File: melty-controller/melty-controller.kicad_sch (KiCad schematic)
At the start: 33 parts, among them J1 Conn_01x02_Male, J2 soicbite, J3 esc_io, Q1 2N7002ET1G, U1 ESP32-PICO-D4, U2 AIC1734-33GUTR, U3 MMA1200KEG, U4 HT7250

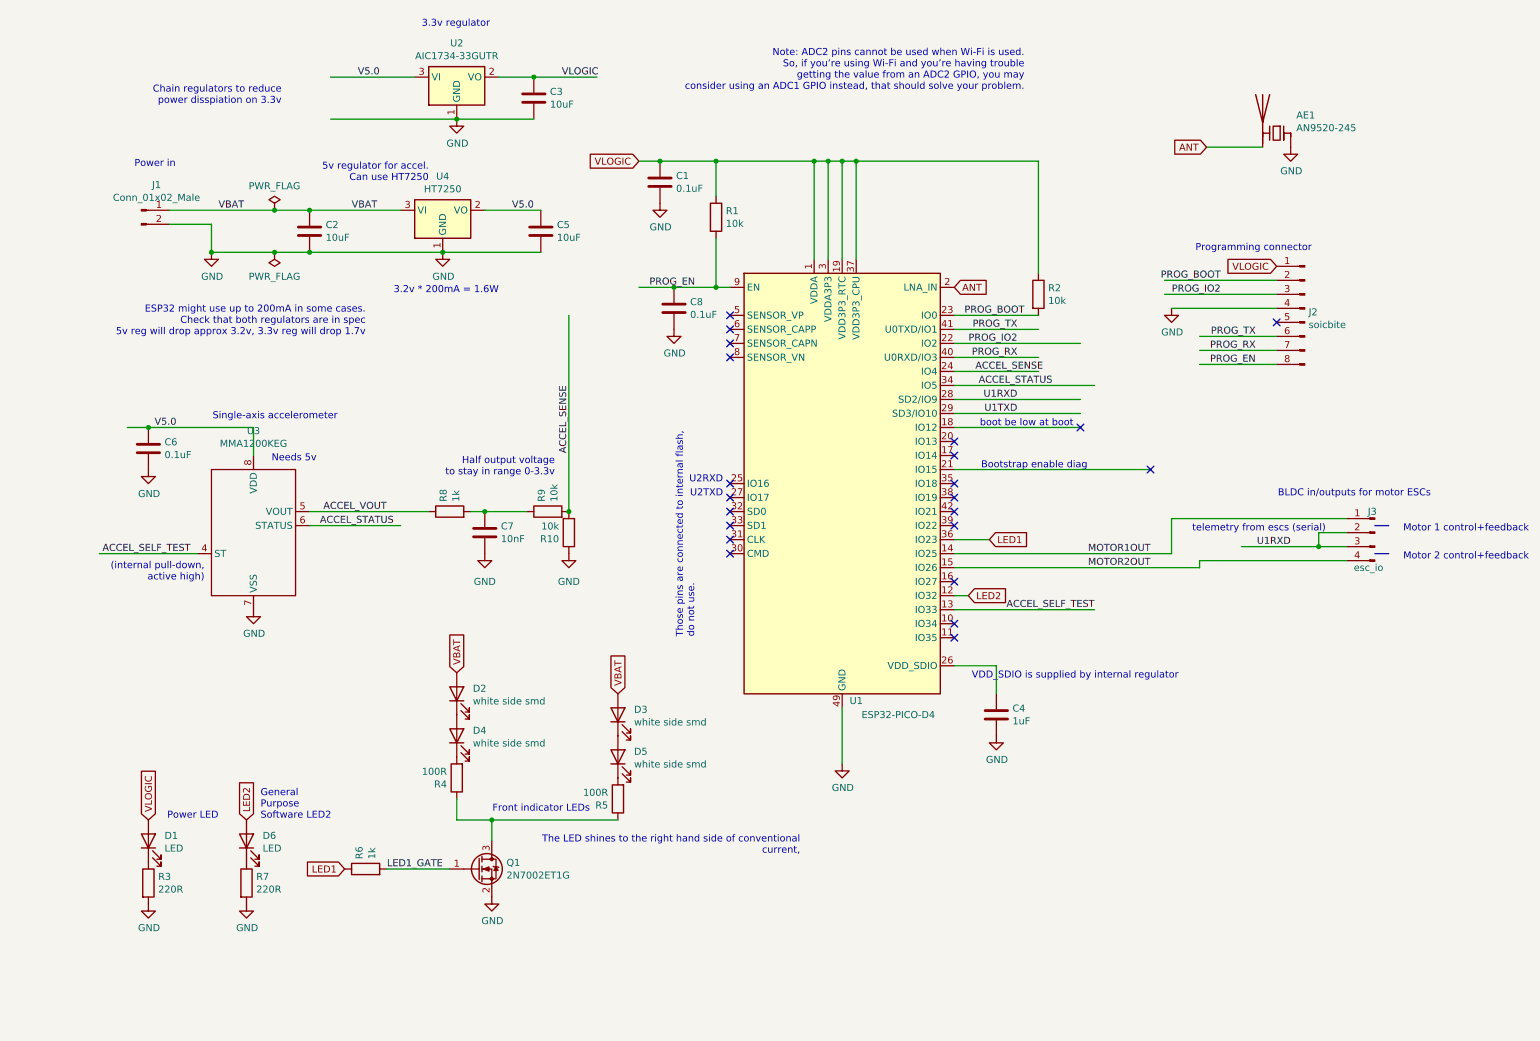
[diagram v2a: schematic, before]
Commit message: clean up net names and stuff
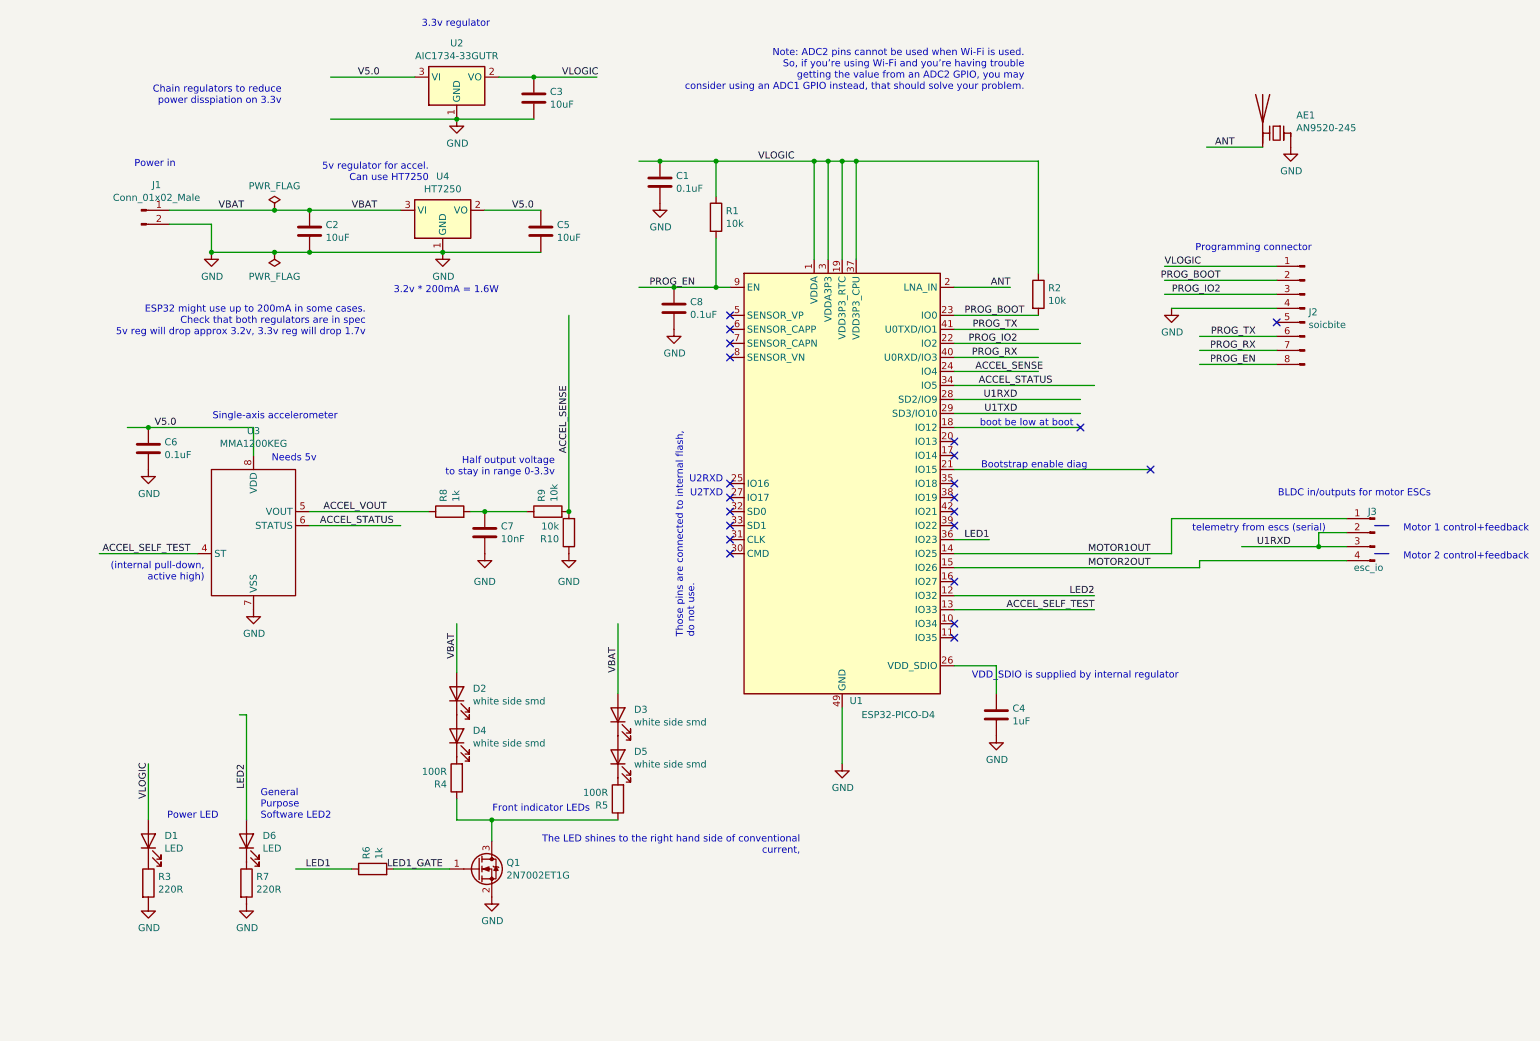
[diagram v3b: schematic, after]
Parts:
- U1: footprint Package_DFN_QFN:QFN-48-1EP_7x7mm_P0.5mm_EP5.3x5.3mm -> melty-controller:esp32-pico-special
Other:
- moved on the sheet: R6
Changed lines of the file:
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@@
   (junction (at 153.67 40.64) (diameter 0) (color 0 0 0 0))
   (junction (at 237.49 110.49) (diameter 0) (color 0 0 0 0))
+  (no_connect (at 130.81 71.12))
+  (no_connect (at 171.45 91.44))
+  (no_connect (at 171.45 116.84))
+  (no_connect (at 229.87 69.85))
+  (no_connect (at 171.45 104.14))
+  (no_connect (at 130.81 73.66))
+  (no_connect (at 171.45 93.98))
+  (no_connect (at 171.45 101.6))
+  (no_connect (at 130.81 106.68))
+  (no_connect (at 171.45 124.46))
+  (no_connect (at 130.81 109.22))
+  (no_connect (at 171.45 127))
+  (no_connect (at 130.81 111.76))
+  (no_connect (at 130.81 68.58))
+  (no_connect (at 130.81 99.06))
+  (no_connect (at 130.81 101.6))
+  (no_connect (at 130.81 104.14))
+  (no_connect (at 171.45 99.06))
+  (no_connect (at 171.45 106.68))
+  (no_connect (at 130.81 76.2))
   (no_connect (at 207.01 96.52))
-  (no_connect (at 130.81 104.14))
-  (no_connect (at 171.45 127))
-  (no_connect (at 171.45 93.98))
-  (no_connect (at 130.81 71.12))
-  (no_connect (at 130.81 106.68))
-  (no_connect (at 130.81 99.06))
-  (no_connect (at 171.45 116.84))
-  (no_connect (at 130.81 111.76))
-  (no_connect (at 130.81 101.6))
-  (no_connect (at 171.45 99.06))
-  (no_connect (at 229.87 69.85))
-  (no_connect (at 171.45 106.68))
-  (no_connect (at 171.45 91.44))
-  (no_connect (at 171.45 101.6))
   (no_connect (at 194.31 88.9))
-  (no_connect (at 130.81 73.66))
-  (no_connect (at 130.81 68.58))
-  (no_connect (at 171.45 104.14))
-  (no_connect (at 130.81 109.22))
-  (no_connect (at 171.45 124.46))
-  (no_connect (at 130.81 76.2))
   (wire (pts (xy 16.51 111.76) (xy 34.29 111.76))
     (stroke (width 0) (type solid) (color 0 0 0 0))
@@
     (stroke (width 0) (type solid) (color 0 0 0 0))
   )
+  (wire (pts (xy 25.4 149.86) (xy 25.4 160.02))
+    (stroke (width 0) (type solid) (color 0 0 0 0))
+  )
   (wire (pts (xy 29.21 49.53) (xy 48.26 49.53))
     (stroke (width 0) (type solid) (color 0 0 0 0))
@@
     (stroke (width 0) (type solid) (color 0 0 0 0))
   )
+  (wire (pts (xy 41.91 140.97) (xy 43.18 140.97))
+    (stroke (width 0) (type solid) (color 0 0 0 0))
+  )
+  (wire (pts (xy 43.18 160.02) (xy 43.18 140.97))
+    (stroke (width 0) (type solid) (color 0 0 0 0))
+  )
   (wire (pts (xy 44.45 93.98) (xy 44.45 88.9))
     (stroke (width 0) (type solid) (color 0 0 0 0))
@@
     (stroke (width 0) (type solid) (color 0 0 0 0))
   )
+  (wire (pts (xy 52.07 168.91) (xy 62.23 168.91))
+    (stroke (width 0) (type solid) (color 0 0 0 0))
+  )
   (wire (pts (xy 54.61 49.53) (xy 71.12 49.53))
     (stroke (width 0) (type solid) (color 0 0 0 0))
@@
     (stroke (width 0) (type solid) (color 0 0 0 0))
   )
-  (wire (pts (xy 68.58 168.91) (xy 80.01 168.91))
+  (wire (pts (xy 69.85 168.91) (xy 80.01 168.91))
     (stroke (width 0) (type solid) (color 0 0 0 0))
   )
@@
     (stroke (width 0) (type solid) (color 0 0 0 0))
   )
+  (wire (pts (xy 81.28 124.46) (xy 81.28 133.35))
+    (stroke (width 0) (type solid) (color 0 0 0 0))
+  )
   (wire (pts (xy 81.28 156.21) (xy 81.28 160.02))
     (stroke (width 0) (type solid) (color 0 0 0 0))
@@
     (stroke (width 0) (type solid) (color 0 0 0 0))
   )
+  (wire (pts (xy 110.49 124.46) (xy 110.49 137.16))
+    (stroke (width 0) (type solid) (color 0 0 0 0))
+  )
   (wire (pts (xy 114.3 63.5) (xy 120.65 63.5))
     (stroke (width 0) (type solid) (color 0 0 0 0))
@@
     (stroke (width 0) (type solid) (color 0 0 0 0))
   )
+  (wire (pts (xy 171.45 63.5) (xy 181.61 63.5))
+    (stroke (width 0) (type solid) (color 0 0 0 0))
+  )
   (wire (pts (xy 171.45 68.58) (xy 186.69 68.58))
     (stroke (width 0) (type solid) (color 0 0 0 0))
@@
     (stroke (width 0) (type solid) (color 0 0 0 0))
   )
-  (wire (pts (xy 171.45 119.38) (xy 173.99 119.38))
+  (wire (pts (xy 171.45 119.38) (xy 196.85 119.38))
     (stroke (width 0) (type solid) (color 0 0 0 0))
   )
@@
   )
   (wire (pts (xy 186.69 60.96) (xy 186.69 40.64))
+    (stroke (width 0) (type solid) (color 0 0 0 0))
+  )
+  (wire (pts (xy 209.55 59.69) (xy 229.87 59.69))
     (stroke (width 0) (type solid) (color 0 0 0 0))
   )
@@
     (effects (font (size 1.27 1.27)) (justify right bottom))
   )
+  (label "VLOGIC" (at 25.4 156.21 90)
+    (effects (font (size 1.27 1.27)) (justify left bottom))
+  )
   (label "V5.0" (at 30.48 88.9 180)
     (effects (font (size 1.27 1.27)) (justify right bottom))
@@
     (effects (font (size 1.27 1.27)) (justify left bottom))
   )
+  (label "LED2" (at 43.18 149.86 270)
+    (effects (font (size 1.27 1.27)) (justify right bottom))
+  )
+  (label "LED1" (at 58.42 168.91 180)
+    (effects (font (size 1.27 1.27)) (justify right bottom))
+  )
   (label "VBAT" (at 62.23 49.53 0)
     (effects (font (size 1.27 1.27)) (justify left bottom))
@@
     (effects (font (size 1.27 1.27)) (justify right bottom))
   )
+  (label "VBAT" (at 81.28 130.81 90)
+    (effects (font (size 1.27 1.27)) (justify left bottom))
+  )
   (label "V5.0" (at 95.25 49.53 180)
     (effects (font (size 1.27 1.27)) (justify right bottom))
@@
     (effects (font (size 1.27 1.27)) (justify right bottom))
   )
+  (label "VBAT" (at 110.49 133.35 90)
+    (effects (font (size 1.27 1.27)) (justify left bottom))
+  )
   (label "PROG_EN" (at 124.46 63.5 180)
     (effects (font (size 1.27 1.27)) (justify right bottom))
+  )
+  (label "VLOGIC" (at 135.89 40.64 0)
+    (effects (font (size 1.27 1.27)) (justify left bottom))
   )
   (label "ACCEL_SENSE" (at 175.26 78.74 0)
     (effects (font (size 1.27 1.27)) (justify left bottom))
   )
+  (label "LED1" (at 177.8 109.22 180)
+    (effects (font (size 1.27 1.27)) (justify right bottom))
+  )
+  (label "ANT" (at 181.61 63.5 180)
+    (effects (font (size 1.27 1.27)) (justify right bottom))
+  )
   (label "PROG_TX" (at 182.88 71.12 180)
     (effects (font (size 1.27 1.27)) (justify right bottom))
@@
     (effects (font (size 1.27 1.27)) (justify right bottom))
   )
+  (label "LED2" (at 196.85 119.38 180)
+    (effects (font (size 1.27 1.27)) (justify right bottom))
+  )
   (label "ACCEL_SELF_TEST" (at 196.85 121.92 180)
     (effects (font (size 1.27 1.27)) (justify right bottom))
@@
     (effects (font (size 1.27 1.27)) (justify right bottom))
   )
+  (label "VLOGIC" (at 209.55 59.69 0)
+    (effects (font (size 1.27 1.27)) (justify left bottom))
+  )
   (label "PROG_BOOT" (at 219.71 62.23 180)
     (effects (font (size 1.27 1.27)) (justify right bottom))
@@
     (effects (font (size 1.27 1.27)) (justify right bottom))
   )
+  (label "ANT" (at 222.25 38.1 180)
+    (effects (font (size 1.27 1.27)) (justify right bottom))
+  )
   (label "PROG_TX" (at 226.06 72.39 180)
     (effects (font (size 1.27 1.27)) (justify right bottom))
@@
   (label "U1RXD" (at 232.41 110.49 180)
     (effects (font (size 1.27 1.27)) (justify right bottom))
-  )
-  (global_label "VLOGIC" (shape input) (at 25.4 160.02 90)
-    (effects (font (size 1.27 1.27)) (justify left))
-  )
-  (global_label "LED2" (shape input) (at 43.18 160.02 90)
-    (effects (font (size 1.27 1.27)) (justify left))
-  )
-  (global_label "LED1" (shape input) (at 60.96 168.91 180)
-    (effects (font (size 1.27 1.27)) (justify right))
-  )
-  (global_label "VBAT" (shape input) (at 81.28 133.35 90)
-    (effects (font (size 1.27 1.27)) (justify left))
-  )
-  (global_label "VBAT" (shape input) (at 110.49 137.16 90)
-    (effects (font (size 1.27 1.27)) (justify left))
-  )
-  (global_label "VLOGIC" (shape input) (at 114.3 40.64 180)
-    (effects (font (size 1.27 1.27)) (justify right))
-  )
-  (global_label "ANT" (shape input) (at 171.45 63.5 0)
-    (effects (font (size 1.27 1.27)) (justify left))
-  )
-  (global_label "LED2" (shape input) (at 173.99 119.38 0)
-    (effects (font (size 1.27 1.27)) (justify left))
-  )
-  (global_label "LED1" (shape input) (at 177.8 109.22 0)
-    (effects (font (size 1.27 1.27)) (justify left))
-  )
-  (global_label "ANT" (shape input) (at 217.17 38.1 180)
-    (effects (font (size 1.27 1.27)) (justify right))
-  )
-  (global_label "VLOGIC" (shape input) (at 229.87 59.69 180)
-    (effects (font (size 1.27 1.27)) (justify right))
   )
   (symbol (lib_id "malenki-nano-rescue:PWR_FLAG-power") (at 48.26 49.53 0) (unit 1)
@@
     )
   )
-  (symbol (lib_id "Device:R") (at 64.77 168.91 90) (unit 1)
-    (in_bom yes) (on_board yes)
-    (property "Reference" "R6" (id 0) (at 63.6206 167.1319 0)
-      (effects (font (size 1.27 1.27)) (justify left))
-    )
-    (property "Value" "1k" (id 1) (at 65.9193 167.1319 0)
-      (effects (font (size 1.27 1.27)) (justify left))
-    )
-    (property "Footprint" "Resistor_SMD:R_0603_1608Metric" (id 2) (at 64.77 170.688 90)
-      (effects (font (size 1.27 1.27)) hide)
-    )
-    (property "Datasheet" "~" (id 3) (at 64.77 168.91 0)
+  (symbol (lib_id "Device:R") (at 66.04 168.91 90) (unit 1)
+    (in_bom yes) (on_board yes)
+    (property "Reference" "R6" (id 0) (at 64.8906 167.1319 0)
+      (effects (font (size 1.27 1.27)) (justify left))
+    )
+    (property "Value" "1k" (id 1) (at 67.1893 167.1319 0)
+      (effects (font (size 1.27 1.27)) (justify left))
+    )
+    (property "Footprint" "Resistor_SMD:R_0603_1608Metric" (id 2) (at 66.04 170.688 90)
+      (effects (font (size 1.27 1.27)) hide)
+    )
+    (property "Datasheet" "~" (id 3) (at 66.04 168.91 0)
       (effects (font (size 1.27 1.27)) hide)
     )
@@
     (property "Reference" "U1" (id 0) (at 153.67 138.43 0))
     (property "Value" "ESP32-PICO-D4" (id 1) (at 161.29 140.97 0))
-    (property "Footprint" "Package_DFN_QFN:QFN-48-1EP_7x7mm_P0.5mm_EP5.3x5.3mm" (id 2) (at 151.13 142.24 0)
-      (effects (font (size 1.27 1.27)) hide)
-    )
+    (property "Footprint" "melty-controller:esp32-pico-special" (id 2) (at 151.13 142.24 0)
+      (effects (font (size 1.27 1.27)) hide)
+    )

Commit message: Fix Antenna footprint; use zener to regulate 5.0v
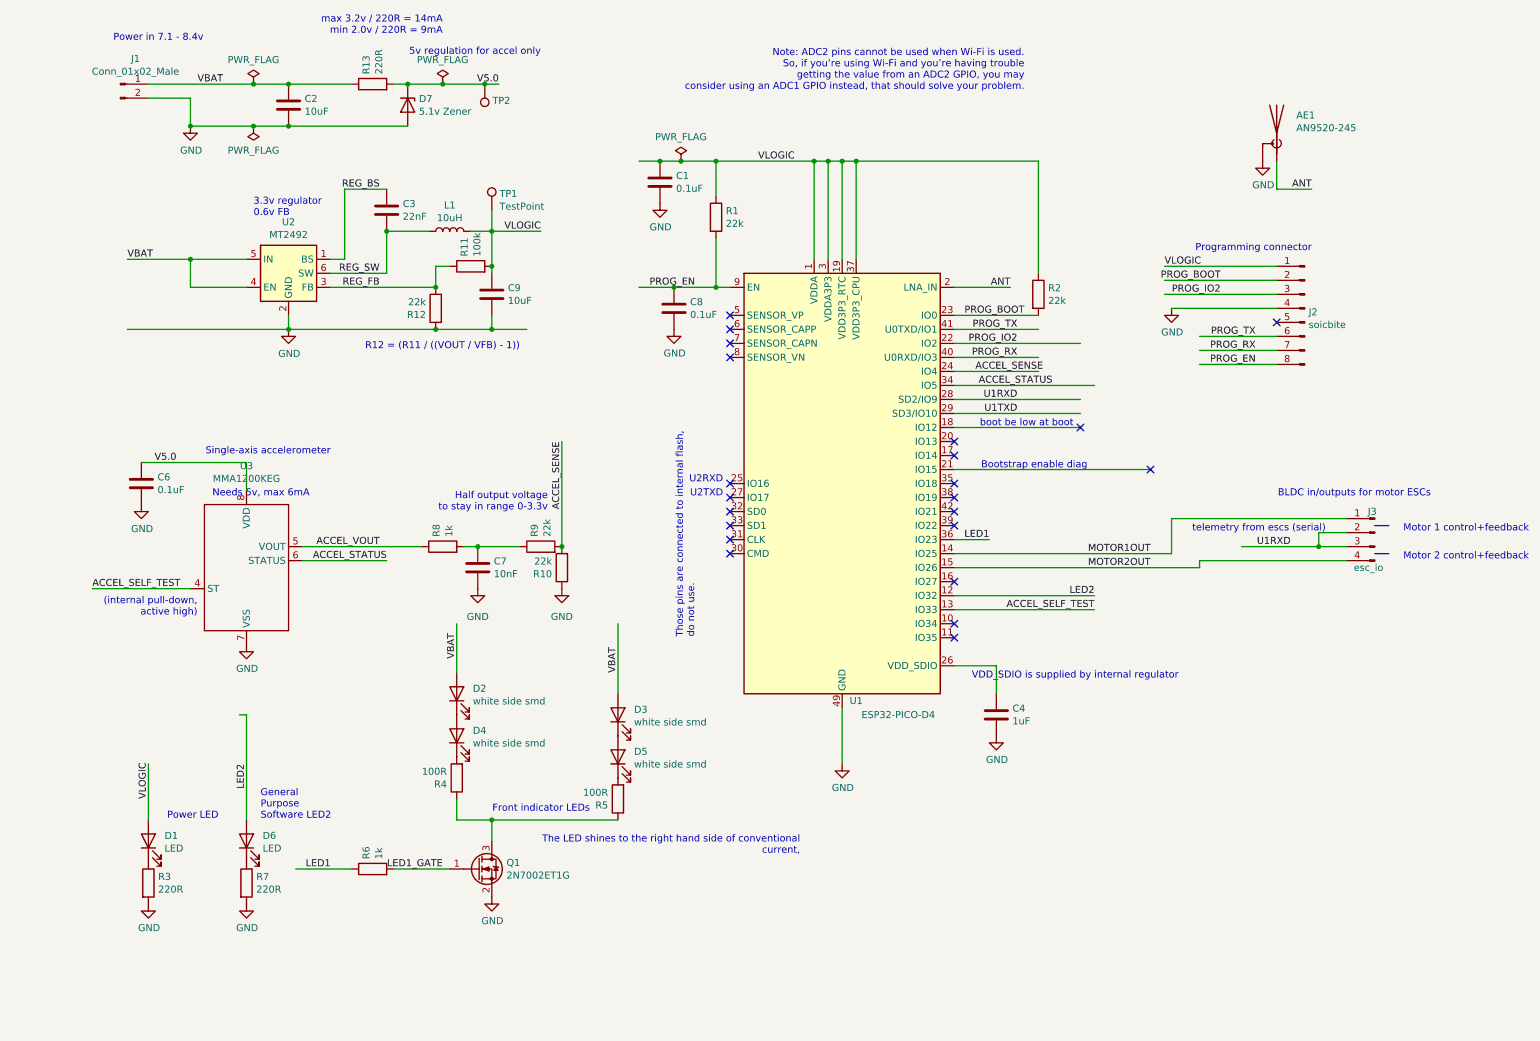
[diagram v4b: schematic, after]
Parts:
- removed C5: 10uF, Capacitor_SMD:C_0603_1608Metric, symbol Device:C
- removed U2: AIC1734-33GUTR, Package_TO_SOT_SMD:SOT-89-3, symbol melty1:HT7233
- removed U4: HT7250, Package_TO_SOT_SMD:SOT-89-3, symbol melty1:HT7233
- added C9: 10uF, Capacitor_SMD:C_0603_1608Metric, symbol Device:C
- added D7: 5.1v Zener, Diode_SMD:D_SOD-323, symbol Device:D_Zener
- added L1: 10uH, Inductor_SMD:L_1210_3225Metric, symbol Device:L
- added R11: 100k, Resistor_SMD:R_0603_1608Metric, symbol Device:R
- added R12: 22k, Resistor_SMD:R_0603_1608Metric, symbol Device:R
- added R13: 220R, Resistor_SMD:R_0603_1608Metric, symbol Device:R
- added TP1, TP2: TestPoint, TestPoint:TestPoint_Pad_1.5x1.5mm, symbol Connector:TestPoint
- added U2: MT2492, Package_TO_SOT_SMD:SOT-23-6, symbol melty1:MT2492
- AE1: footprint RF_Antenna:Johanson_2450AT43F0100 -> melty-controller:AN9520-245; symbol Device:Antenna_Chip -> Device:Antenna_Shield
- C3: value 10uF -> 22nF; LCSC C19702 -> (none)
- R1, R10, R2, R9: value 10k -> 22k
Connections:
- net ANT: now also AE1.1 (A); no longer AE1.2 (PCB_Trace)
- net GND: now also AE1.2 (Shield), C9.2, D7.2 (A), R12.1, U2.2 (GND); no longer AE1.1 (FEED), C3.2
- net V5.0: now also D7.1 (K), R13.2, TP2.1
- net VBAT: now also R13.1, U2.4 (EN), U2.5 (IN)
- net VLOGIC: now also C9.1, L1.2, R11.2, TP1.1; no longer C3.1
- new net REG_BS: C3.1, U2.1 (BS)
- new net REG_FB: R11.1, R12.2, U2.3 (FB)
- new net REG_SW: C3.2, L1.1, U2.6 (SW)
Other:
- note added: "3.3v regulator 0.6v FB"
- note added: "5v regulation for accel only"
- note added: "Needs 5v, max 6mA"
- note added: "Power in 7.1 - 8.4v"
- note added: "R12 = (R11 / ((VOUT / VFB) - 1))"
- note added: "max 3.2v / 220R = 14mA min 2.0v / 220R = 9mA"
- note removed: "3.2v * 200mA = 1.6W"
- note removed: "3.3v regulator"
- note removed: "5v regulator for accel. Can use HT7250"
- note removed: "Chain regulators to reduce power disspiation on 3.3v"
- note removed: "ESP32 might use up to 200mA in some cases. Check that both regulators are in spec 5v reg will drop approx 3.2v, 3.3v reg will drop 1.7v"
- note removed: "Needs 5v"
- note removed: "Power in"
- moved on the sheet: AE1, C2, C6, C7, J1, R10, R8, R9, U3
